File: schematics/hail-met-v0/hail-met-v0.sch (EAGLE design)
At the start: 104 parts, among them IC1 MCP73871, J1 AVR_SPI_PRG_6PTH, U1 ATMEGA328P, Y1 16MHZ

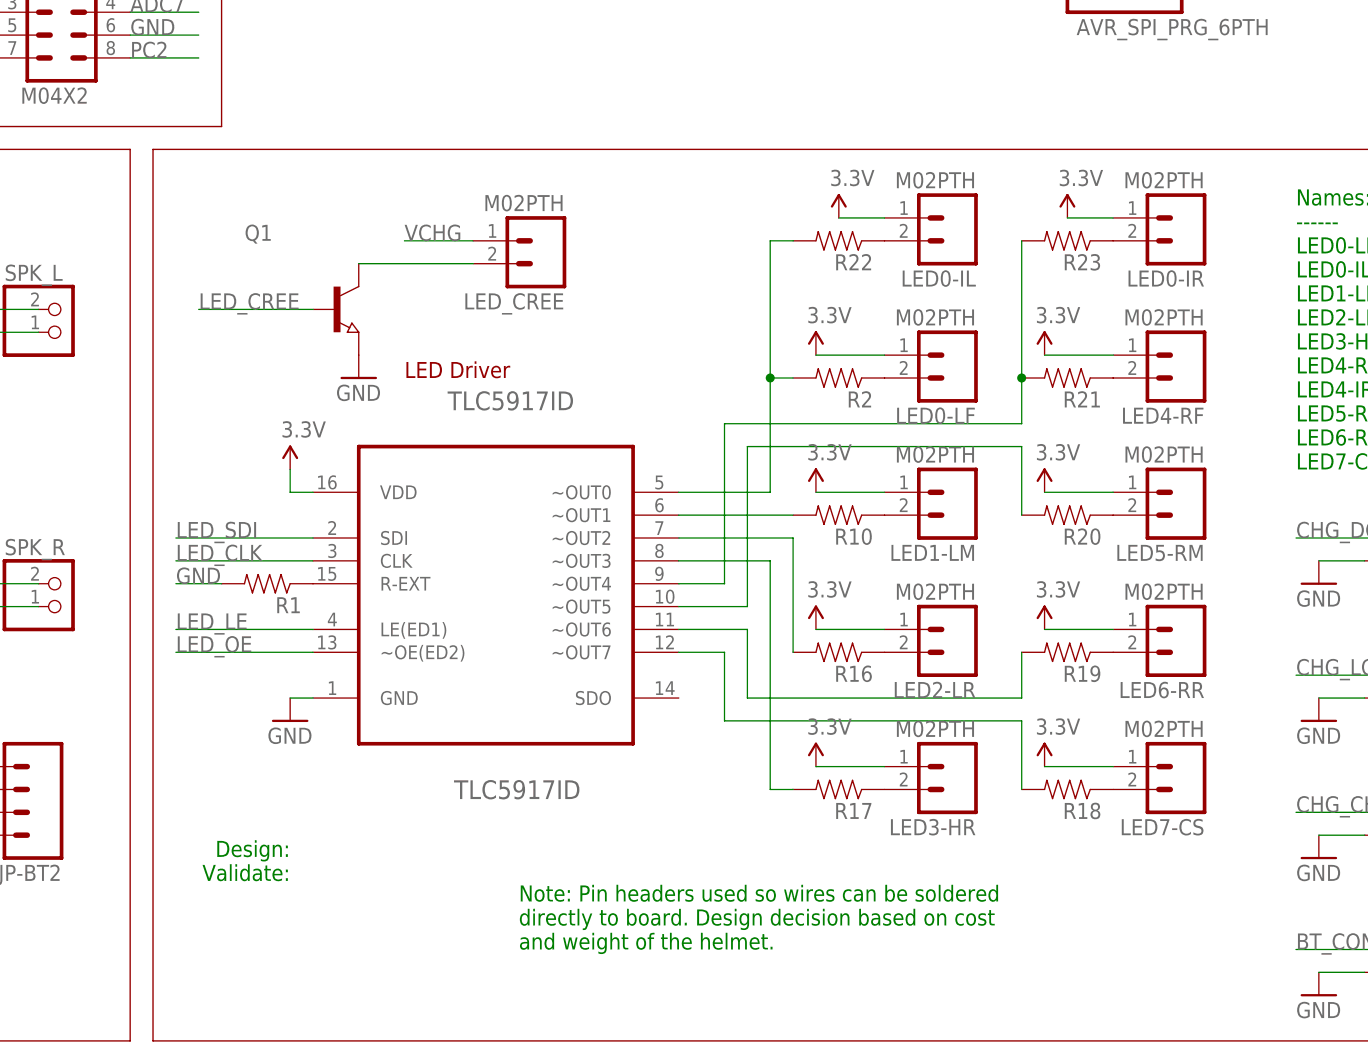
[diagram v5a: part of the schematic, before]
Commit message: added pull-down for transistor
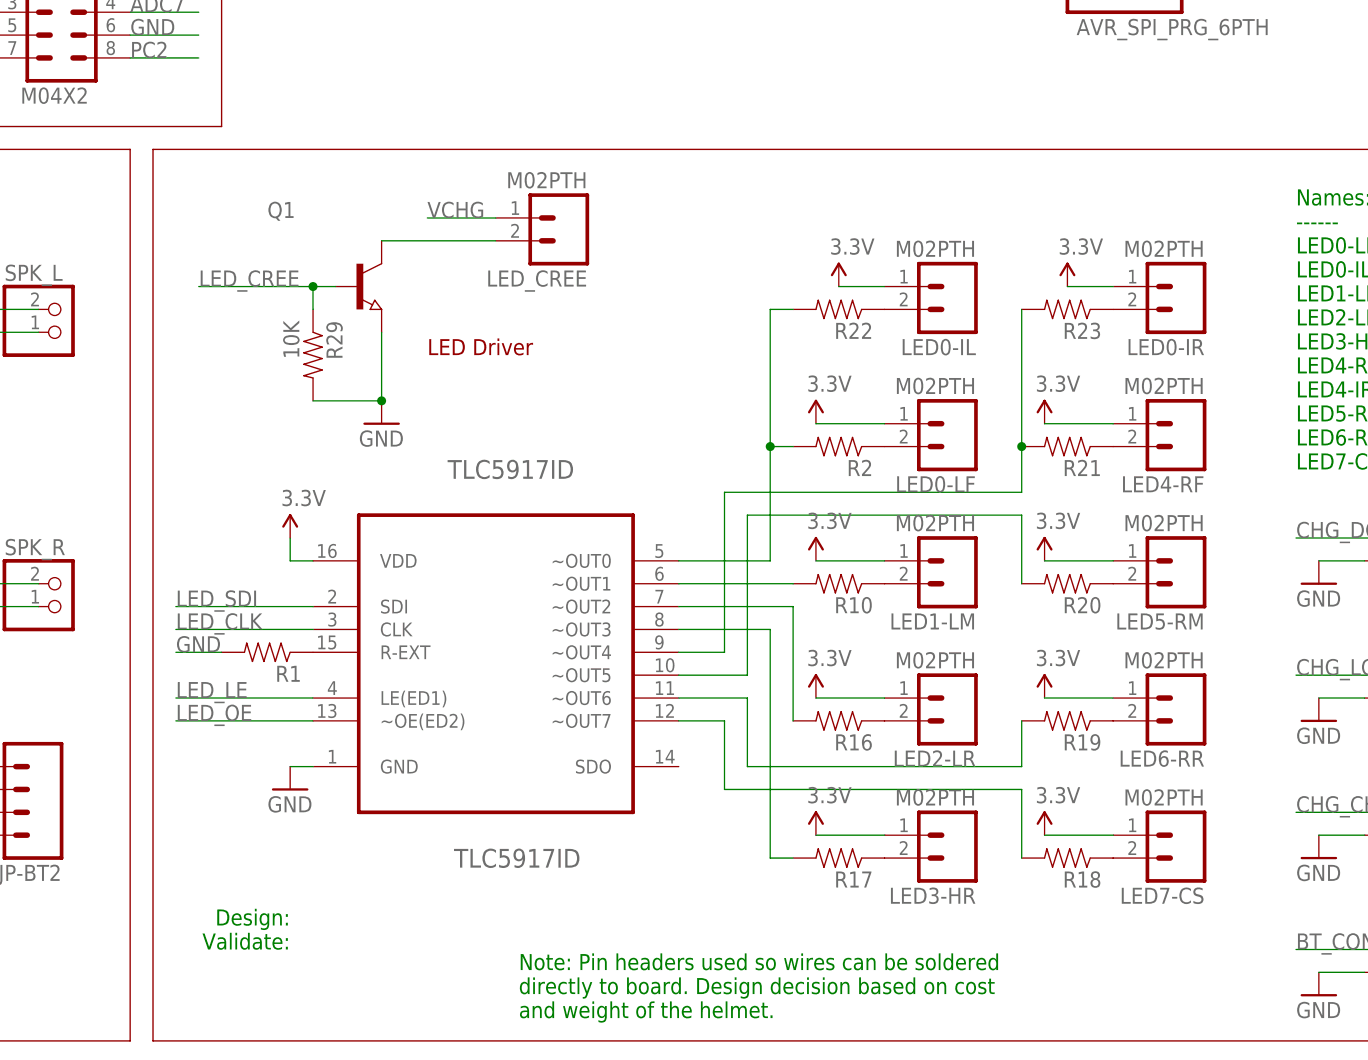
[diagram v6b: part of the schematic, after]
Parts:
- added R29: 10K, SparkFun-Passives:RESISTOR0805-RES
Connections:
- net GND: now also R29.2
- net LED_CREE: now also R29.1
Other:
- moved on the sheet: LED0-IL, LED0-IR, LED0-LF, LED1-LM, LED2-LR, LED3-HR, LED4-RF, LED5-RM, LED6-RR, LED7-CS, LED_CREE, Q1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

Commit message: added some decoupling caps to the board, prep for ben
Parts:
- added C10, C11, C12, C13, C14: (no value), SparkFun-Capacitors:CAP_POLPTH1
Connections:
- net 3.3V: now also C10.+, C11.+, C12.+, C13.+, C14.+
- net CHG_VOUT: now also LED_CREE.1
- net GND: now also C10.-, C11.-, C12.-, C13.-, C14.-
- net VCHG: no longer LED_CREE.1
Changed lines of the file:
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@@
 <?xml version="1.0" encoding="utf-8"?>
 <!DOCTYPE eagle SYSTEM "eagle.dtd">
-<eagle version="7.1.0">
+<eagle version="6.5.0">
 <drawing>
 <settings>
@@
 <part name="GND41" library="SparkFun" deviceset="GND" device=""/>
 <part name="R29" library="SparkFun-Passives" deviceset="RESISTOR" device="0805-RES" value="10K"/>
+<part name="C10" library="SparkFun-Capacitors" deviceset="CAP_POL" device="PTH1"/>
+<part name="C11" library="SparkFun-Capacitors" deviceset="CAP_POL" device="PTH1"/>
+<part name="C12" library="SparkFun-Capacitors" deviceset="CAP_POL" device="PTH1"/>
+<part name="C13" library="SparkFun-Capacitors" deviceset="CAP_POL" device="PTH1"/>
+<part name="C14" library="SparkFun-Capacitors" deviceset="CAP_POL" device="PTH1"/>
+<part name="GND42" library="SparkFun" deviceset="GND" device=""/>
 </parts>
 <sheets>
@@
 <instance part="GND41" gate="1" x="-60.96" y="38.1"/>
 <instance part="R29" gate="G$1" x="71.12" y="-30.48" rot="R270"/>
+<instance part="C10" gate="G$1" x="-40.64" y="60.96"/>
+<instance part="C11" gate="G$1" x="-30.48" y="60.96"/>
+<instance part="C12" gate="G$1" x="-20.32" y="60.96"/>
+<instance part="C13" gate="G$1" x="-10.16" y="60.96"/>
+<instance part="C14" gate="G$1" x="-50.8" y="60.96"/>
+<instance part="GND42" gate="1" x="-22.86" y="50.8"/>
 </instances>
 <busses>
@@
 <pinref part="GND41" gate="1" pin="GND"/>
 </segment>
+<segment>
+<pinref part="C14" gate="G$1" pin="-"/>
+<pinref part="C10" gate="G$1" pin="-"/>
+<wire x1="-50.8" y1="55.88" x2="-40.64" y2="55.88" width="0.1524" layer="91"/>
+<pinref part="C11" gate="G$1" pin="-"/>
+<wire x1="-40.64" y1="55.88" x2="-30.48" y2="55.88" width="0.1524" layer="91"/>
+<junction x="-40.64" y="55.88"/>
+<pinref part="C12" gate="G$1" pin="-"/>
+<wire x1="-30.48" y1="55.88" x2="-20.32" y2="55.88" width="0.1524" layer="91"/>
+<junction x="-30.48" y="55.88"/>
+<pinref part="C13" gate="G$1" pin="-"/>
+<wire x1="-20.32" y1="55.88" x2="-10.16" y2="55.88" width="0.1524" layer="91"/>
+<junction x="-20.32" y="55.88"/>
+<pinref part="GND42" gate="1" pin="GND"/>
+<wire x1="-22.86" y1="53.34" x2="-20.32" y2="53.34" width="0.1524" layer="91"/>
+<wire x1="-20.32" y1="53.34" x2="-20.32" y2="55.88" width="0.1524" layer="91"/>
+</segment>
 </net>
 <net name="VIN" class="0">
@@
 <label x="27.94" y="10.16" size="1.778" layer="95"/>
 </segment>
+<segment>
+<pinref part="C14" gate="G$1" pin="+"/>
+<pinref part="C10" gate="G$1" pin="+"/>
+<wire x1="-50.8" y1="63.5" x2="-40.64" y2="63.5" width="0.1524" layer="91"/>
+<pinref part="C11" gate="G$1" pin="+"/>
+<wire x1="-40.64" y1="63.5" x2="-30.48" y2="63.5" width="0.1524" layer="91"/>
+<junction x="-40.64" y="63.5"/>
+<pinref part="C12" gate="G$1" pin="+"/>
+<wire x1="-30.48" y1="63.5" x2="-20.32" y2="63.5" width="0.1524" layer="91"/>
+<junction x="-30.48" y="63.5"/>
+<pinref part="C13" gate="G$1" pin="+"/>
+<wire x1="-20.32" y1="63.5" x2="-10.16" y2="63.5" width="0.1524" layer="91"/>
+<junction x="-20.32" y="63.5"/>
+<wire x1="-30.48" y1="63.5" x2="-30.48" y2="66.04" width="0.1524" layer="91"/>
+<label x="-30.48" y="66.04" size="1.778" layer="95"/>
+</segment>
 </net>
 <net name="RXD" class="0">
@@
 <pinref part="R3" gate="G$1" pin="2"/>
 </segment>
-<segment>
-<pinref part="LED_CREE" gate="G$1" pin="1"/>
-<wire x1="83.82" y1="-15.24" x2="91.44" y2="-15.24" width="0.1524" layer="91"/>
-<label x="83.82" y="-15.24" size="1.778" layer="95"/>
-</segment>
 </net>
 <net name="N$18" class="0">
@@
 <pinref part="JP-BT3" gate="G$1" pin="1"/>
 </segment>
-</net>
+<segment>
+<pinref part="LED_CREE" gate="G$1" pin="1"/>
+<wire x1="83.82" y1="-15.24" x2="91.44" y2="-15.24" width="0.1524" layer="91"/>
+<label x="78.74" y="-15.24" size="1.778" layer="95"/>
+</segment>
+</net>

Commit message: finalized board design, added new npn datasheet
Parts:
- Q1: device semicon-smd-ipc:NPN-TRANSISTOR_SOT89 -> SparkFun:TRANSISTOR_NPNSOT23-3
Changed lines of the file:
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@@
 <?xml version="1.0" encoding="utf-8"?>
 <!DOCTYPE eagle SYSTEM "eagle.dtd">
-<eagle version="6.5.0">
+<eagle version="7.1.0">
 <drawing>
 <settings>
@@
 <part name="SPK_L" library="adafruit" deviceset="JST_2PIN" device="-SMT"/>
 <part name="SPK_R" library="adafruit" deviceset="JST_2PIN" device="-SMT"/>
-<part name="Q1" library="semicon-smd-ipc" deviceset="NPN-TRANSISTOR_" device="SOT89"/>
 <part name="GND17" library="SparkFun" deviceset="GND" device=""/>
 <part name="JP-BT2" library="SparkFun-Connectors" deviceset="M04" device="LOCK"/>
@@
 <part name="C14" library="SparkFun-Capacitors" deviceset="CAP_POL" device="PTH1"/>
 <part name="GND42" library="SparkFun" deviceset="GND" device=""/>
+<part name="Q1" library="SparkFun" deviceset="TRANSISTOR_NPN" device="SOT23-3"/>
 </parts>
 <sheets>
@@
 <instance part="SPK_L" gate="G$1" x="43.18" y="-27.94"/>
 <instance part="SPK_R" gate="G$1" x="43.18" y="-58.42"/>
-<instance part="Q1" gate="G$1" x="76.2" y="-22.86"/>
 <instance part="GND17" gate="1" x="78.74" y="-38.1"/>
 <instance part="JP-BT2" gate="G$1" x="38.1" y="-78.74" rot="R180"/>
@@
 <instance part="C14" gate="G$1" x="-50.8" y="60.96"/>
 <instance part="GND42" gate="1" x="-22.86" y="50.8"/>
+<instance part="Q1" gate="G$1" x="76.2" y="-22.86"/>
 </instances>
 <busses>
@@
 </segment>
 <segment>
-<pinref part="Q1" gate="G$1" pin="E"/>
 <pinref part="GND17" gate="1" pin="GND"/>
 <wire x1="78.74" y1="-35.56" x2="78.74" y2="-27.94" width="0.1524" layer="91"/>
@@
 <wire x1="78.74" y1="-35.56" x2="71.12" y2="-35.56" width="0.1524" layer="91"/>
 <junction x="78.74" y="-35.56"/>
+<pinref part="Q1" gate="G$1" pin="E"/>
 </segment>
 <segment>
@@
 <net name="N$19" class="0">
 <segment>
-<pinref part="Q1" gate="G$1" pin="C"/>
 <pinref part="LED_CREE" gate="G$1" pin="2"/>
 <wire x1="91.44" y1="-17.78" x2="78.74" y2="-17.78" width="0.1524" layer="91"/>
+<pinref part="Q1" gate="G$1" pin="C"/>
 </segment>
 </net>
@@
 </segment>
 <segment>
-<pinref part="Q1" gate="G$1" pin="B"/>
 <wire x1="73.66" y1="-22.86" x2="71.12" y2="-22.86" width="0.1524" layer="91"/>
 <pinref part="R29" gate="G$1" pin="1"/>
@@
 <junction x="71.12" y="-22.86"/>
 <label x="58.42" y="-22.86" size="1.778" layer="95"/>
-</segment>
-</net>
+<pinref part="Q1" gate="G$1" pin="B"/>
+</segment>
+</net>
